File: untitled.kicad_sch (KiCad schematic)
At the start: 1 part

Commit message: completed rev1 of PCB layout
need to double check components and other elements, connections, and add values
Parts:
- removed Mic1: Here for custom footprint, MEMS_Mic_SMD:Mic_SMD_0603_1608Metric, symbol Device:R
- added U2: SPV08A0LR5H-1, MEMS_Mic_SMD:SPV08A0LR5H-1, symbol SPV08A0LR5H-1:SPV08A0LR5H-1
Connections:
- net 1_VDD: now also U2.VDDA
- net 2_OUT: now also U2.OUT
- net 3_GND: now also U2.AGND
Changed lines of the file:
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@@
 (kicad_sch (version 20230121) (generator eeschema)
   (paper "A4")
-  (hierarchical_label "3_GND" (shape output) (at 134.62 107.95 0) (fields_autoplaced)
+  (hierarchical_label "3_GND" (shape output) (at 149.86 105.41 180) (fields_autoplaced)
+    (effects (font (size 1.27 1.27)) (justify right))
+  )
+  (hierarchical_label "1_VDD" (shape input) (at 149.86 100.33 180) (fields_autoplaced)
+    (effects (font (size 1.27 1.27)) (justify right))
+  )
+  (hierarchical_label "2_OUT" (shape output) (at 170.18 102.87 0) (fields_autoplaced)
     (effects (font (size 1.27 1.27)) (justify left))
   )
-  (hierarchical_label "1_VDD" (shape input) (at 134.62 102.87 0) (fields_autoplaced)
-    (effects (font (size 1.27 1.27)) (justify left))
-  )
-  (hierarchical_label "2_OUT" (shape output) (at 134.62 111.76 0) (fields_autoplaced)
-    (effects (font (size 1.27 1.27)) (justify left))
-  )
-  (symbol (lib_id "Device:R") (at 152.4 105.41 0) (unit 1)
+  (symbol (lib_id "SPV08A0LR5H-1:SPV08A0LR5H-1") (at 154.94 105.41 0) (unit 1)
     (in_bom yes) (on_board yes) (dnp no) (fields_autoplaced)
-    (property "Reference" "Mic1" (at 154.94 104.14 0)
-      (effects (font (size 1.27 1.27)) (justify left))
+    (property "Reference" "U2" (at 160.02 92.71 0)
+      (effects (font (size 1.27 1.27)))
     )
-    (property "Value" "Here for custom footprint" (at 154.94 106.68 0)
-      (effects (font (size 1.27 1.27)) (justify left))
+    (property "Value" "SPV08A0LR5H-1" (at 160.02 95.25 0)
+      (effects (font (size 1.27 1.27)))
     )
-    (property "Footprint" "MEMS_Mic_SMD:Mic_SMD_0603_1608Metric" (at 150.622 105.41 90)
+    (property "Footprint" "MEMS_Mic_SMD:SPV08A0LR5H-1" (at 154.94 105.41 0)
+      (effects (font (size 1.27 1.27)) (justify bottom) hide)
+    )
+    (property "Datasheet" "" (at 154.94 105.41 0)
       (effects (font (size 1.27 1.27)) hide)
     )
-    (property "Datasheet" "~" (at 152.4 105.41 0)
-      (effects (font (size 1.27 1.27)) hide)
-    )
-    (pin "1")
-    (pin "2")
+    (pin "AGND")
+    (pin "OUT")
+    (pin "VDDA")
     (instances
       (project "VibeLight"
         (path "/704dec10-a4c2-4298-be85-193d9407f59f/964563b4-99e1-4b3d-857d-35f5fde5aa09/2471d6e6-9095-48a0-a82f-426dd1cde29c"
-          (reference "Mic1") (unit 1)
+          (reference "U2") (unit 1)
         )
       )

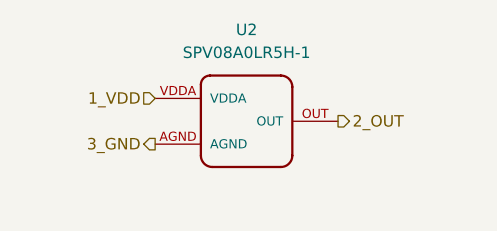
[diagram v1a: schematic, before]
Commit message: new pcb rev with updated audio filter
The only ERC and DRC warnings/errors are unconnected pins and silkscreen text issues. There are two DRC issues that have to do with the mic, but I don't think they're an issue
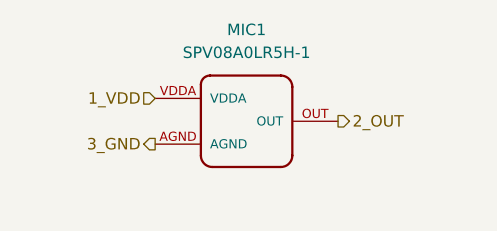
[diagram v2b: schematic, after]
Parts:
- renumbered U2 to MIC1
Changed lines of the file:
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@@
   (symbol (lib_id "SPV08A0LR5H-1:SPV08A0LR5H-1") (at 154.94 105.41 0) (unit 1)
     (in_bom yes) (on_board yes) (dnp no) (fields_autoplaced)
-    (property "Reference" "U2" (at 160.02 92.71 0)
+    (property "Reference" "MIC1" (at 160.02 92.71 0)
       (effects (font (size 1.27 1.27)))
     )
@@
       (project "VibeLight"
         (path "/704dec10-a4c2-4298-be85-193d9407f59f/964563b4-99e1-4b3d-857d-35f5fde5aa09/2471d6e6-9095-48a0-a82f-426dd1cde29c"
-          (reference "U2") (unit 1)
+          (reference "MIC1") (unit 1)
         )
       )
